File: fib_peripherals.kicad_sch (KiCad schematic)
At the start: 1 part, among them J801 Conn_02x20_Odd_Even

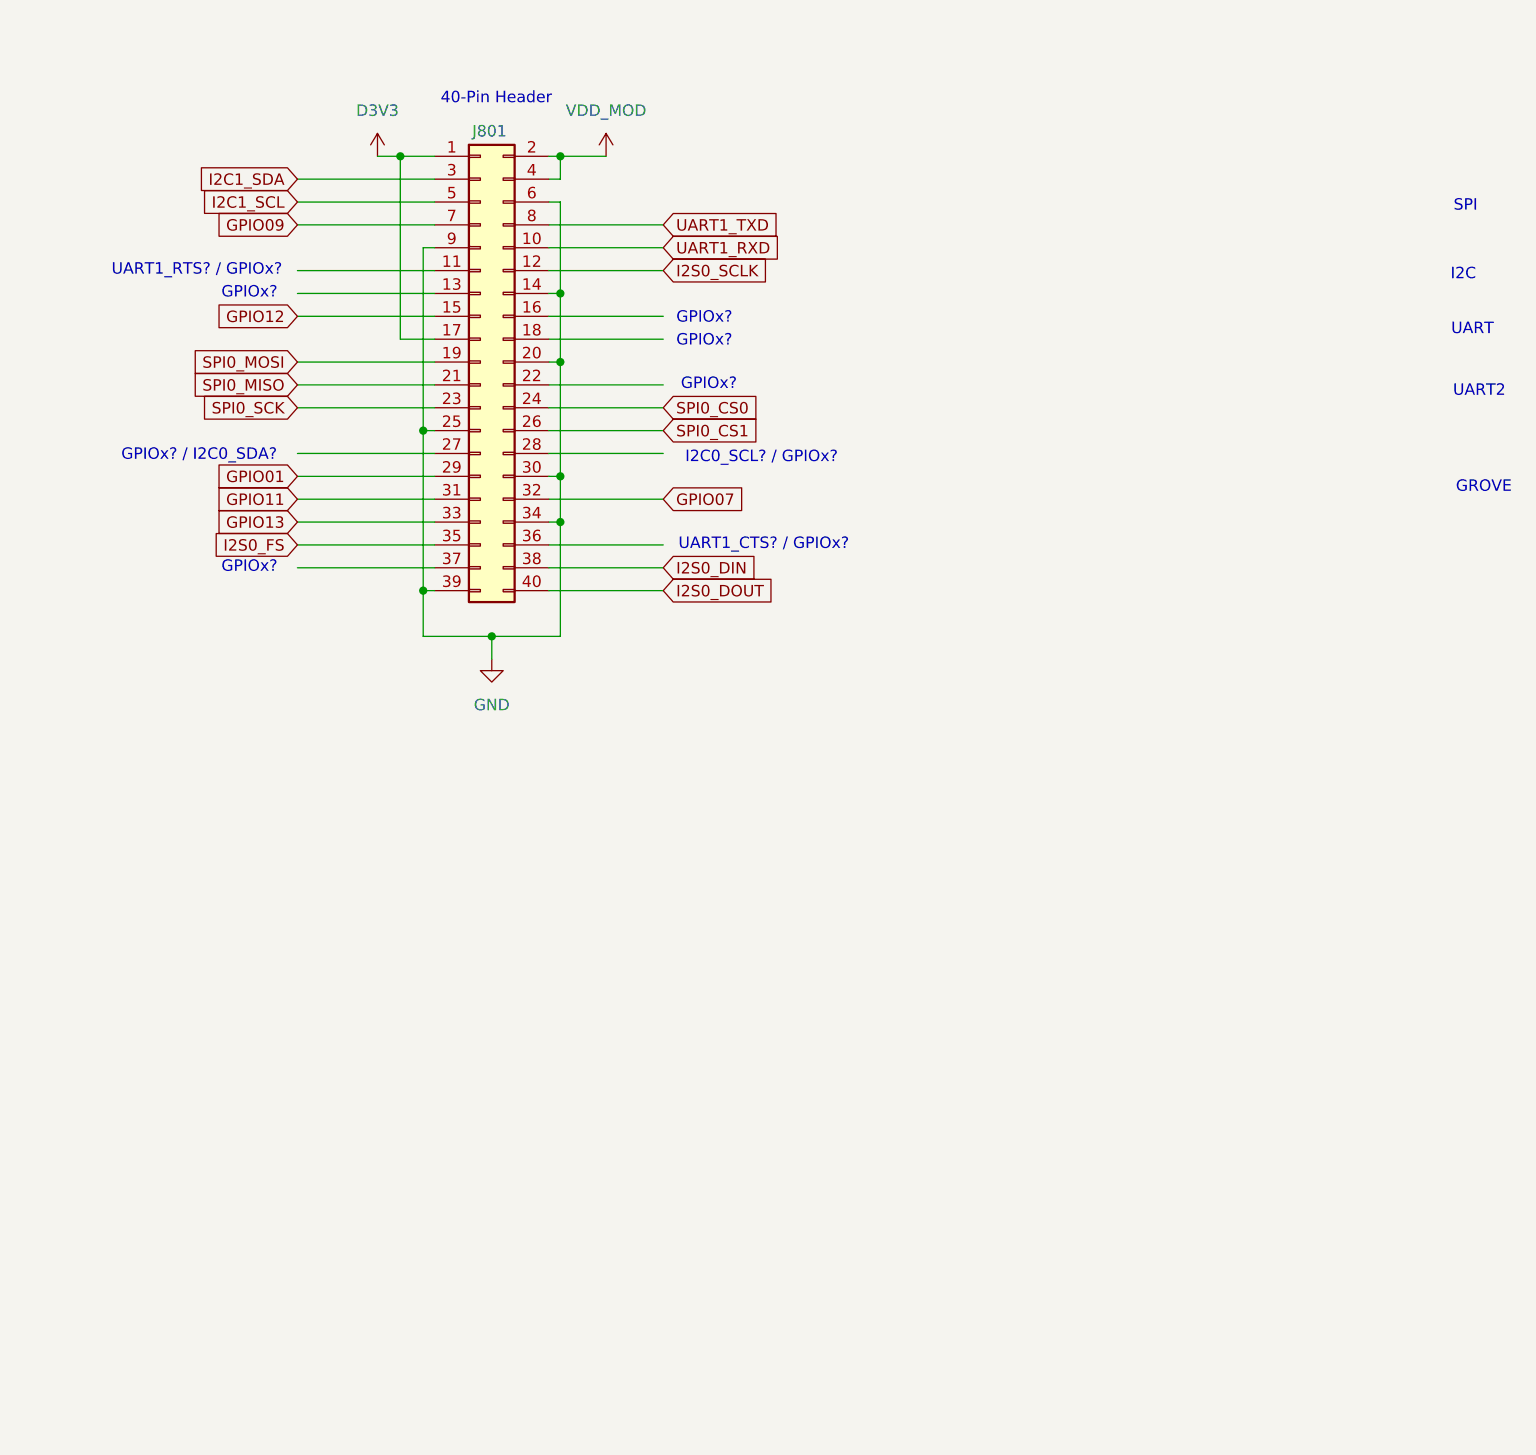
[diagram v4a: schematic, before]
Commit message: added buck converter, refactoored peripherals and updated gpio/SPI/i2c mapping
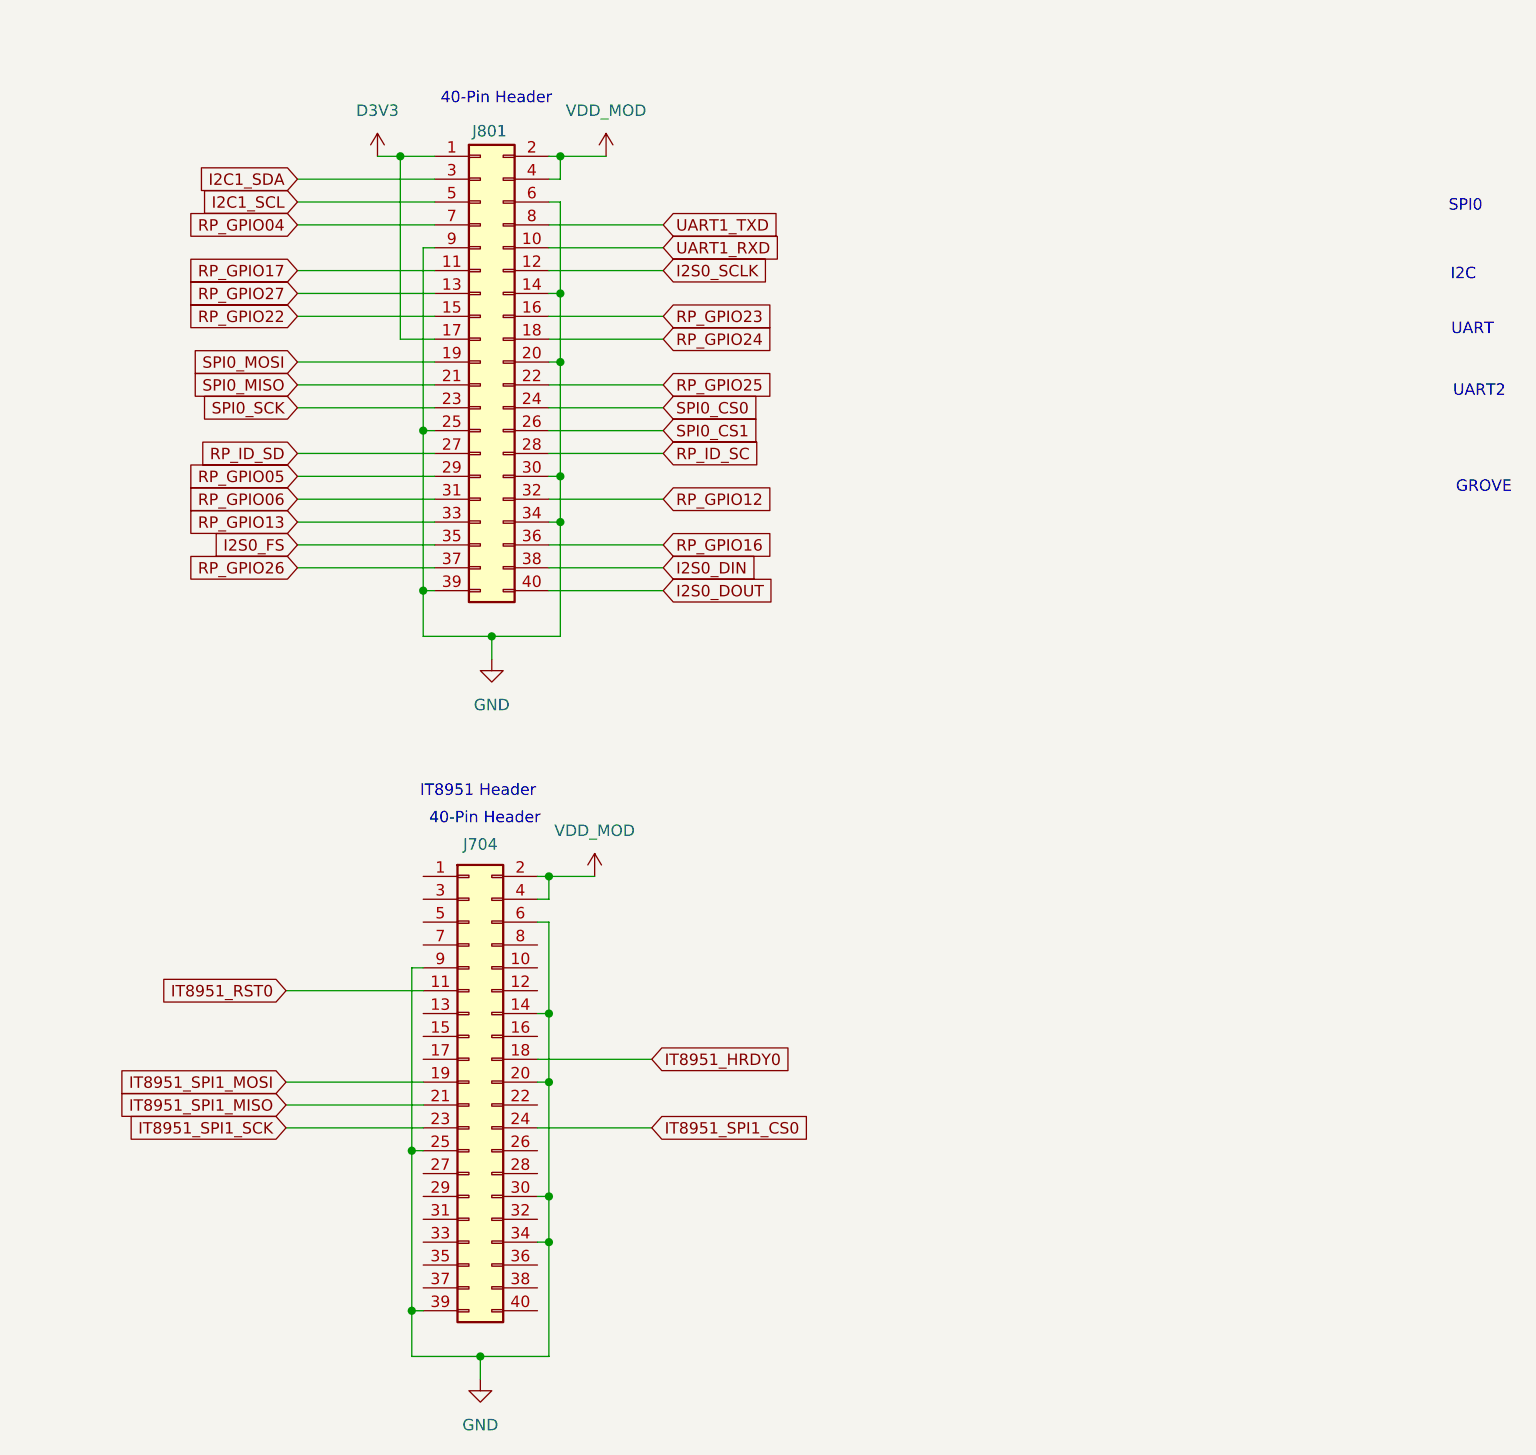
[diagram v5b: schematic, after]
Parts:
- added J704: Conn_02x20_Odd_Even, Connector_PinHeader_2.54mm:PinHeader_2x20_P2.54mm_Vertical, symbol Connector_Generic:Conn_02x20_Odd_Even
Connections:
- net GND: now also J704.14 (Pin_14), J704.20 (Pin_20), J704.25 (Pin_25), J704.30 (Pin_30), J704.34 (Pin_34), J704.39 (Pin_39), J704.6 (Pin_6), J704.9 (Pin_9)
- net VDD_MOD: now also J704.2 (Pin_2), J704.4 (Pin_4)
- net RP_GPIO17: now reaches J801.11 (Pin_11)
- net RP_GPIO27: now reaches J801.13 (Pin_13)
- net RP_GPIO23: now reaches J801.16 (Pin_16)
- net RP_GPIO24: now reaches J801.18 (Pin_18)
- net RP_GPIO25: now reaches J801.22 (Pin_22)
- net RP_ID_SD: now reaches J801.27 (Pin_27)
- net RP_ID_SC: now reaches J801.28 (Pin_28)
- net RP_GPIO16: now reaches J801.36 (Pin_36)
- net RP_GPIO26: now reaches J801.37 (Pin_37)
- net GPIO01 renamed RP_GPIO05
- net GPIO07 renamed RP_GPIO12
- net GPIO09 renamed RP_GPIO04
- net GPIO11 renamed RP_GPIO06
- net GPIO12 renamed RP_GPIO22
- net GPIO13 renamed RP_GPIO13
- new net IT8951_HRDY0: J704.18 (Pin_18)
- new net IT8951_RST0: J704.11 (Pin_11)
- new net IT8951_SPI1_CS0: J704.24 (Pin_24)
- new net IT8951_SPI1_MISO: J704.21 (Pin_21)
- new net IT8951_SPI1_MOSI: J704.19 (Pin_19)
- new net IT8951_SPI1_SCK: J704.23 (Pin_23)
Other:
- note added: "IT8951 Header"
- note added: "SPI0"
- note removed: "GPIOx?"
- note removed: "GPIOx? / I2C0_SDA?"
- note removed: "I2C0_SCL? / GPIOx?"
- note removed: "SPI"
- note removed: "UART1_CTS? / GPIOx?"
- note removed: "UART1_RTS? / GPIOx?"

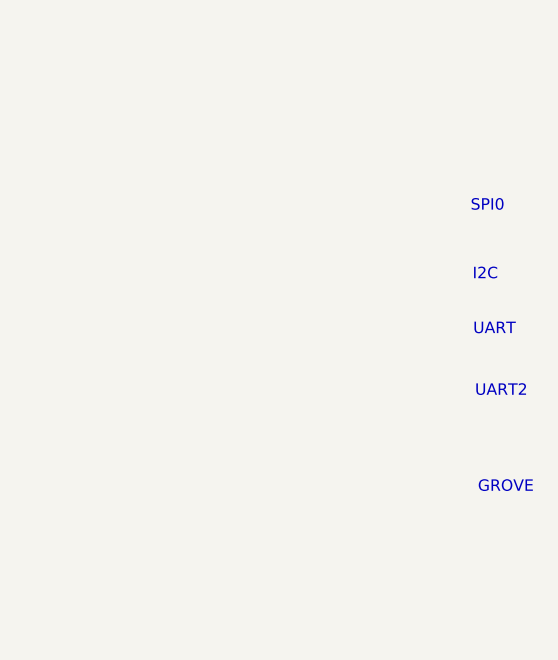
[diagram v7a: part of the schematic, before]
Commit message: refactored PCIe pages
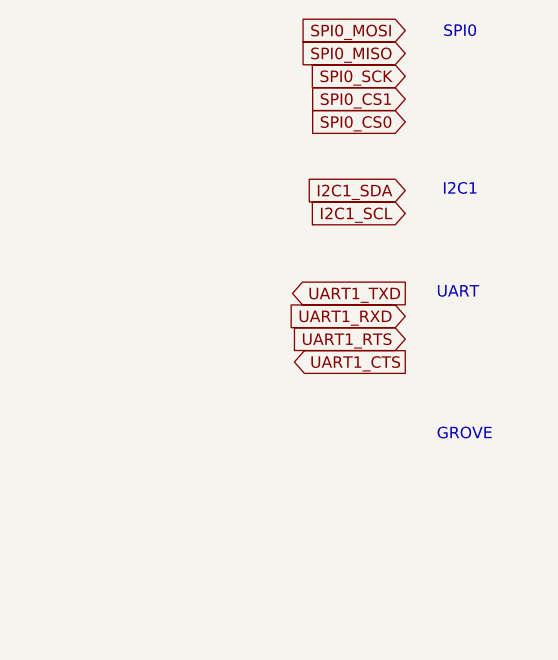
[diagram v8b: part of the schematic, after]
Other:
- note added: "I2C1"
- note removed: "I2C"
- note removed: "UART2"
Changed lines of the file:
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@@
 		)
 	)
-	(text "I2C"
+	(text "I2C1"
 		(exclude_from_sim no)
-		(at 175.26 52.578 0)
+		(at 172.466 43.18 0)
 		(effects
 			(font
@@
 	(text "UART"
 		(exclude_from_sim no)
-		(at 176.276 58.674 0)
+		(at 172.212 54.61 0)
 		(effects
 			(font
@@
 	(text "GROVE"
 		(exclude_from_sim no)
-		(at 177.546 76.2 0)
+		(at 172.974 70.358 0)
 		(effects
 			(font
@@
 		)
 	)
-	(text "UART2"
-		(exclude_from_sim no)
-		(at 177.038 65.532 0)
-		(effects
-			(font
-				(size 1.27 1.27)
-			)
-		)
-	)
 	(text "40-Pin Header"
 		(exclude_from_sim no)
@@
 	(text "SPI0"
 		(exclude_from_sim no)
-		(at 175.514 44.958 0)
+		(at 172.466 25.654 0)
 		(effects
 			(font
@@
 		)
 	)
+	(global_label "UART1_RTS"
+		(shape input)
+		(at 166.37 59.69 180)
+		(effects
+			(font
+				(size 1.27 1.27)
+			)
+			(justify right)
+		)
+		(property "Intersheetrefs" "${INTERSHEET_REFS}"
+			(at 152.4 59.69 0)
+			(effects
+				(font
+					(size 1.27 1.27)
+				)
+				(justify right)
+				(hide yes)
+			)
+		)
+	)
 	(global_label "RP_GPIO26"
 		(shape input)
@@
 		)
 	)
+	(global_label "I2C1_SDA"
+		(shape input)
+		(at 166.37 43.18 180)
+		(fields_autoplaced yes)
+		(effects
+			(font
+				(size 1.27 1.27)
+			)
+			(justify right)
+		)
+		(property "Intersheetrefs" "${INTERSHEET_REFS}"
+			(at 154.5553 43.18 0)
+			(effects
+				(font
+					(size 1.27 1.27)
+				)
+				(justify right)
+				(hide yes)
+			)
+		)
+	)
 	(global_label "IT8951_HRDY0"
 		(shape input)
@@
 		)
 	)
+	(global_label "UART1_RXD"
+		(shape input)
+		(at 166.37 57.15 180)
+		(effects
+			(font
+				(size 1.27 1.27)
+			)
+			(justify right)
+		)
+		(property "Intersheetrefs" "${INTERSHEET_REFS}"
+			(at 152.4 57.15 0)
+			(effects
+				(font
+					(size 1.27 1.27)
+				)
+				(justify right)
+				(hide yes)
+			)
+		)
+	)
 	(global_label "RP_GPIO06"
 		(shape input)
@@
 		)
 	)
+	(global_label "I2C1_SCL"
+		(shape input)
+		(at 166.37 45.72 180)
+		(fields_autoplaced yes)
+		(effects
+			(font
+				(size 1.27 1.27)
+			)
+			(justify right)
+		)
+		(property "Intersheetrefs" "${INTERSHEET_REFS}"
+			(at 154.6158 45.72 0)
+			(effects
+				(font
+					(size 1.27 1.27)
+				)
+				(justify right)
+				(hide yes)
+			)
+		)
+	)
 	(global_label "RP_ID_SC"
 		(shape input)
@@
 		)
 	)
+	(global_label "SPI0_SCK"
+		(shape input)
+		(at 166.37 30.48 180)
+		(fields_autoplaced yes)
+		(effects
+			(font
+				(size 1.27 1.27)
+			)
+			(justify right)
+		)
+		(property "Intersheetrefs" "${INTERSHEET_REFS}"
+			(at 154.3739 30.48 0)
+			(effects
+				(font
+					(size 1.27 1.27)
+				)
+				(justify right)
+				(hide yes)
+			)
+		)
+	)
 	(global_label "I2S0_DOUT"
 		(shape input)
@@
 		)
 	)
+	(global_label "SPI0_MOSI"
+		(shape input)
+		(at 166.37 25.4 180)
+		(fields_autoplaced yes)
+		(effects
+			(font
+				(size 1.27 1.27)
+			)
+			(justify right)
+		)
+		(property "Intersheetrefs" "${INTERSHEET_REFS}"
+			(at 153.5272 25.4 0)
+			(effects
+				(font
+					(size 1.27 1.27)
+				)
+				(justify right)
+				(hide yes)
+			)
+		)
+	)
 	(global_label "RP_GPIO16"
 		(shape input)
@@
 		)
 	)
+	(global_label "SPI0_CS0"
+		(shape input)
+		(at 166.37 35.56 180)
+		(fields_autoplaced yes)
+		(effects
+			(font
+				(size 1.27 1.27)
+			)
+			(justify right)
+		)
+		(property "Intersheetrefs" "${INTERSHEET_REFS}"
+			(at 154.4344 35.56 0)
+			(effects
+				(font
+					(size 1.27 1.27)
+				)
+				(justify right)
+				(hide yes)
+			)
+		)
+	)
 	(global_label "RP_GPIO24"
 		(shape input)
@@
 		)
 	)
+	(global_label "SPI0_CS1"
+		(shape input)
+		(at 166.37 33.02 180)
+		(fields_autoplaced yes)
+		(effects
+			(font
+				(size 1.27 1.27)
+			)
+			(justify right)
+		)
+		(property "Intersheetrefs" "${INTERSHEET_REFS}"
+			(at 154.4344 33.02 0)
+			(effects
+				(font
+					(size 1.27 1.27)
+				)
+				(justify right)
+				(hide yes)
+			)
+		)
+	)
 	(global_label "RP_GPIO25"
 		(shape input)
@@
 		)
 	)
+	(global_label "UART1_CTS"
+		(shape output)
+		(at 166.37 62.23 180)
+		(effects
+			(font
+				(size 1.27 1.27)
+			)
+			(justify right)
+		)
+		(property "Intersheetrefs" "${INTERSHEET_REFS}"
+			(at 152.4 62.23 0)
+			(effects
+				(font
+					(size 1.27 1.27)
+				)
+				(justify right)
+				(hide yes)
+			)
+		)
+	)
+	(global_label "UART1_TXD"
+		(shape output)
+		(at 166.37 54.61 180)
+		(effects
+			(font
+				(size 1.27 1.27)
+			)
+			(justify right)
+		)
+		(property "Intersheetrefs" "${INTERSHEET_REFS}"
+			(at 152.4 54.61 0)
+			(effects
+				(font
+					(size 1.27 1.27)
+				)
+				(justify right)
+				(hide yes)
+			)
+		)
+	)
 	(global_label "SPI0_MOSI"
 		(shape input)
@@
 			(effects
 				(font
+					(size 1.27 1.27)
+				)
+				(justify right)
+				(hide yes)
+			)
+		)
+	)
+	(global_label "SPI0_MISO"
+		(shape input)
+		(at 166.37 27.94 180)
+		(fields_autoplaced yes)
+		(effects
+			(font
+				(size 1.27 1.27)
+			)
+			(justify right)
+		)
+		(property "Intersheetrefs" "${INTERSHEET_REFS}"
+			(at 153.5272 27.94 0)
+			(effects
+				(font
